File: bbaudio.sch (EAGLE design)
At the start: 35 parts, among them U1 V_REG_MIC2920, U2 V_REG_MIC2920, U3 LMZ14203

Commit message: Some more tewaks to the power section
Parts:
- removed C3: 1uF, rcl:C-EUC0603
- removed C4: 10uF, sparkfun:CAP_POL1206
- removed U1: V_REG_MIC2920, sparkfun:V_REG_MIC2920
- added C10: 10uF, sparkfun:CAP_POL1206
- added C7: 1uF, rcl:C-EUC0603
- added U4: VREG, nonolith:VREG
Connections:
- new net VCC: C2.+, U2.OUT
- net +12V: now also C1.1, U2.IN
- net 1.8V: now also C7.1, U4.VIN; no longer C4.+, U1.OUT
- net 3.3V: now also C10.+, U4.VO; no longer C2.+, C3.1, U1.IN, U2.OUT
- net 5V: no longer C1.1, U2.IN
- net GND: now also C10.-, C7.2, U4.GND; no longer C3.2, C4.-, U1.GND
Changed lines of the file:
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@@
 <part name="R9" library="SparkFun-Passives" deviceset="RESISTOR" device="0603-RES" value="56"/>
 <part name="FRAME1" library="SparkFun-Aesthetics" deviceset="FRAME-LETTER" device=""/>
-<part name="C3" library="rcl" deviceset="C-EU" device="C0603" value="1uF"/>
-<part name="C4" library="sparkfun" deviceset="CAP_POL" device="1206" value="10uF"/>
-<part name="GND7" library="sparkfun" deviceset="GND" device=""/>
-<part name="P+5" library="sparkfun" deviceset="3.3V" device=""/>
-<part name="U1" library="sparkfun" deviceset="V_REG_MIC2920" device=""/>
 <part name="U$10" library="sparkfun" deviceset="1.8V" device=""/>
 <part name="C1" library="rcl" deviceset="C-EU" device="C0603" value="1uF"/>
 <part name="C2" library="sparkfun" deviceset="CAP_POL" device="1206" value="10uF"/>
 <part name="GND2" library="sparkfun" deviceset="GND" device=""/>
-<part name="P+1" library="sparkfun" deviceset="3.3V" device=""/>
 <part name="U2" library="sparkfun" deviceset="V_REG_MIC2920" device=""/>
-<part name="U$3" library="sparkfun" deviceset="5V" device=""/>
 <part name="U3" library="SparkFun-PowerIC" deviceset="LMZ14203" device=""/>
 <part name="C5" library="sparkfun" deviceset="CAP_POL" device="1206" value="10uF"/>
@@
 <part name="R4" library="SparkFun-Passives" deviceset="RESISTOR" device="0603-RES" value="1.07k"/>
 <part name="U$4" library="sparkfun" deviceset="5V" device=""/>
+<part name="P+7" library="supply1" deviceset="+12V" device=""/>
+<part name="P+1" library="supply1" deviceset="VCC" device="" value="AVCC"/>
+<part name="C7" library="rcl" deviceset="C-EU" device="C0603" value="1uF"/>
+<part name="C10" library="sparkfun" deviceset="CAP_POL" device="1206" value="10uF"/>
+<part name="GND12" library="sparkfun" deviceset="GND" device=""/>
+<part name="P+8" library="sparkfun" deviceset="3.3V" device=""/>
+<part name="U4" library="nonolith" deviceset="VREG" device=""/>
+<part name="GND13" library="sparkfun" deviceset="GND" device=""/>
 </parts>
 <sheets>
@@
 <instance part="FRAME1" gate="G$1" x="-78.74" y="-109.22"/>
 <instance part="FRAME1" gate="G$2" x="68.58" y="-109.22"/>
-<instance part="C3" gate="G$1" x="-25.4" y="-142.24"/>
-<instance part="C4" gate="G$1" x="0" y="-142.24"/>
-<instance part="GND7" gate="1" x="-12.7" y="-154.94"/>
-<instance part="P+5" gate="G$1" x="-25.4" y="-129.54" rot="MR0"/>
-<instance part="U1" gate="G$1" x="-12.7" y="-134.62"/>
-<instance part="U$10" gate="G$1" x="0" y="-129.54"/>
+<instance part="U$10" gate="G$1" x="-30.48" y="-127"/>
 <instance part="C1" gate="G$1" x="-73.66" y="-142.24"/>
 <instance part="C2" gate="G$1" x="-48.26" y="-142.24"/>
 <instance part="GND2" gate="1" x="-60.96" y="-154.94"/>
-<instance part="P+1" gate="G$1" x="-48.26" y="-129.54" rot="MR0"/>
 <instance part="U2" gate="G$1" x="-60.96" y="-134.62"/>
-<instance part="U$3" gate="G$1" x="-73.66" y="-129.54"/>
 <instance part="U3" gate="G$1" x="-40.64" y="-185.42"/>
 <instance part="C5" gate="G$1" x="-76.2" y="-200.66"/>
@@
 <instance part="R4" gate="G$1" x="-17.78" y="-203.2" rot="R90"/>
 <instance part="U$4" gate="G$1" x="0" y="-172.72"/>
+<instance part="P+7" gate="1" x="-73.66" y="-127"/>
+<instance part="P+1" gate="VCC" x="-48.26" y="-127"/>
+<instance part="C7" gate="G$1" x="-30.48" y="-142.24"/>
+<instance part="C10" gate="G$1" x="-2.54" y="-142.24"/>
+<instance part="GND12" gate="1" x="-17.78" y="-154.94"/>
+<instance part="P+8" gate="G$1" x="-2.54" y="-127" rot="MR0"/>
+<instance part="U4" gate="G$1" x="-17.78" y="-134.62" rot="MR180"/>
+<instance part="GND13" gate="1" x="-5.08" y="-134.62"/>
 </instances>
 <busses>
@@
 <wire x1="137.16" y1="-2.54" x2="157.48" y2="-2.54" width="0.1524" layer="91"/>
 <wire x1="157.48" y1="-2.54" x2="157.48" y2="-7.62" width="0.1524" layer="91"/>
-</segment>
-<segment>
-<wire x1="0" y1="-149.86" x2="0" y2="-147.32" width="0.1524" layer="91"/>
-<wire x1="-12.7" y1="-149.86" x2="0" y2="-149.86" width="0.1524" layer="91"/>
-<wire x1="-12.7" y1="-149.86" x2="-12.7" y2="-152.4" width="0.1524" layer="91"/>
-<wire x1="-12.7" y1="-149.86" x2="-25.4" y2="-149.86" width="0.1524" layer="91"/>
-<wire x1="-25.4" y1="-149.86" x2="-25.4" y2="-147.32" width="0.1524" layer="91"/>
-<wire x1="-12.7" y1="-142.24" x2="-12.7" y2="-149.86" width="0.1524" layer="91"/>
-<junction x="-12.7" y="-149.86"/>
-<pinref part="C3" gate="G$1" pin="2"/>
-<pinref part="GND7" gate="1" pin="GND"/>
-<pinref part="C4" gate="G$1" pin="-"/>
-<pinref part="U1" gate="G$1" pin="GND"/>
 </segment>
 <segment>
@@
 <wire x1="0" y1="-190.5" x2="0" y2="-200.66" width="0.1524" layer="91"/>
 </segment>
+<segment>
+<wire x1="-2.54" y1="-149.86" x2="-2.54" y2="-147.32" width="0.1524" layer="91"/>
+<wire x1="-17.78" y1="-149.86" x2="-2.54" y2="-149.86" width="0.1524" layer="91"/>
+<wire x1="-17.78" y1="-149.86" x2="-17.78" y2="-152.4" width="0.1524" layer="91"/>
+<wire x1="-17.78" y1="-149.86" x2="-30.48" y2="-149.86" width="0.1524" layer="91"/>
+<wire x1="-30.48" y1="-149.86" x2="-30.48" y2="-147.32" width="0.1524" layer="91"/>
+<junction x="-17.78" y="-149.86"/>
+<pinref part="C7" gate="G$1" pin="2"/>
+<pinref part="GND12" gate="1" pin="GND"/>
+<pinref part="C10" gate="G$1" pin="-"/>
+</segment>
+<segment>
+<wire x1="-7.62" y1="-132.08" x2="-5.08" y2="-132.08" width="0.1524" layer="91"/>
+<pinref part="U4" gate="G$1" pin="GND"/>
+<pinref part="GND13" gate="1" pin="GND"/>
+</segment>
 </net>
 <net name="1.8V" class="0">
@@
 </segment>
 <segment>
-<wire x1="0" y1="-139.7" x2="0" y2="-134.62" width="0.1524" layer="91"/>
-<wire x1="0" y1="-134.62" x2="-5.08" y2="-134.62" width="0.1524" layer="91"/>
-<pinref part="C4" gate="G$1" pin="+"/>
-<pinref part="U1" gate="G$1" pin="OUT"/>
+<wire x1="-30.48" y1="-139.7" x2="-30.48" y2="-134.62" width="0.1524" layer="91"/>
+<wire x1="-30.48" y1="-134.62" x2="-27.94" y2="-134.62" width="0.1524" layer="91"/>
+<pinref part="C7" gate="G$1" pin="1"/>
+<pinref part="U4" gate="G$1" pin="VIN"/>
 <pinref part="U$10" gate="G$1" pin="1.8V"/>
-<wire x1="0" y1="-129.54" x2="0" y2="-134.62" width="0.1524" layer="91"/>
-<junction x="0" y="-134.62"/>
+<wire x1="-30.48" y1="-127" x2="-30.48" y2="-134.62" width="0.1524" layer="91"/>
+<junction x="-30.48" y="-134.62"/>
 </segment>
 </net>
@@
 </segment>
 <segment>
-<wire x1="-25.4" y1="-139.7" x2="-25.4" y2="-134.62" width="0.1524" layer="91"/>
-<wire x1="-25.4" y1="-134.62" x2="-20.32" y2="-134.62" width="0.1524" layer="91"/>
-<pinref part="C3" gate="G$1" pin="1"/>
-<pinref part="U1" gate="G$1" pin="IN"/>
-<pinref part="P+5" gate="G$1" pin="3.3V"/>
-<wire x1="-25.4" y1="-129.54" x2="-25.4" y2="-134.62" width="0.1524" layer="91"/>
-<junction x="-25.4" y="-134.62"/>
-</segment>
-<segment>
-<wire x1="-48.26" y1="-139.7" x2="-48.26" y2="-134.62" width="0.1524" layer="91"/>
-<wire x1="-48.26" y1="-134.62" x2="-53.34" y2="-134.62" width="0.1524" layer="91"/>
-<pinref part="C2" gate="G$1" pin="+"/>
-<pinref part="U2" gate="G$1" pin="OUT"/>
-<pinref part="P+1" gate="G$1" pin="3.3V"/>
-<wire x1="-48.26" y1="-129.54" x2="-48.26" y2="-134.62" width="0.1524" layer="91"/>
-<junction x="-48.26" y="-134.62"/>
+<wire x1="-2.54" y1="-139.7" x2="-2.54" y2="-137.16" width="0.1524" layer="91"/>
+<wire x1="-7.62" y1="-137.16" x2="-2.54" y2="-137.16" width="0.1524" layer="91"/>
+<junction x="-2.54" y="-137.16"/>
+<pinref part="C10" gate="G$1" pin="+"/>
+<pinref part="U4" gate="G$1" pin="VO"/>
+<pinref part="P+8" gate="G$1" pin="3.3V"/>
+<wire x1="-2.54" y1="-127" x2="-2.54" y2="-137.16" width="0.1524" layer="91"/>
 </segment>
 </net>
@@
 <pinref part="U$7" gate="G$1" pin="5V"/>
 <wire x1="81.28" y1="-7.62" x2="71.12" y2="-7.62" width="0.1524" layer="91"/>
-</segment>
-<segment>
-<wire x1="-73.66" y1="-139.7" x2="-73.66" y2="-134.62" width="0.1524" layer="91"/>
-<wire x1="-73.66" y1="-134.62" x2="-68.58" y2="-134.62" width="0.1524" layer="91"/>
-<pinref part="C1" gate="G$1" pin="1"/>
-<pinref part="U2" gate="G$1" pin="IN"/>
-<pinref part="U$3" gate="G$1" pin="5V"/>
-<wire x1="-73.66" y1="-129.54" x2="-73.66" y2="-134.62" width="0.1524" layer="91"/>
-<junction x="-73.66" y="-134.62"/>
 </segment>
 <segment>
@@
 <junction x="-76.2" y="-193.04"/>
 </segment>
+<segment>
+<wire x1="-73.66" y1="-139.7" x2="-73.66" y2="-134.62" width="0.1524" layer="91"/>
+<wire x1="-73.66" y1="-134.62" x2="-68.58" y2="-134.62" width="0.1524" layer="91"/>
+<pinref part="C1" gate="G$1" pin="1"/>
+<pinref part="U2" gate="G$1" pin="IN"/>
+<pinref part="P+7" gate="1" pin="+12V"/>
+<wire x1="-73.66" y1="-129.54" x2="-73.66" y2="-134.62" width="0.1524" layer="91"/>
+<junction x="-73.66" y="-134.62"/>
+</segment>
 </net>
 <net name="N$6" class="0">
@@
 </segment>
 </net>
+<net name="VCC" class="0">
+<segment>
+<wire x1="-48.26" y1="-139.7" x2="-48.26" y2="-134.62" width="0.1524" layer="91"/>
+<wire x1="-48.26" y1="-134.62" x2="-53.34" y2="-134.62" width="0.1524" layer="91"/>
+<pinref part="C2" gate="G$1" pin="+"/>
+<pinref part="U2" gate="G$1" pin="OUT"/>
+<pinref part="P+1" gate="VCC" pin="VCC"/>
+<wire x1="-48.26" y1="-129.54" x2="-48.26" y2="-134.62" width="0.1524" layer="91"/>
+<junction x="-48.26" y="-134.62"/>
+</segment>
+</net>

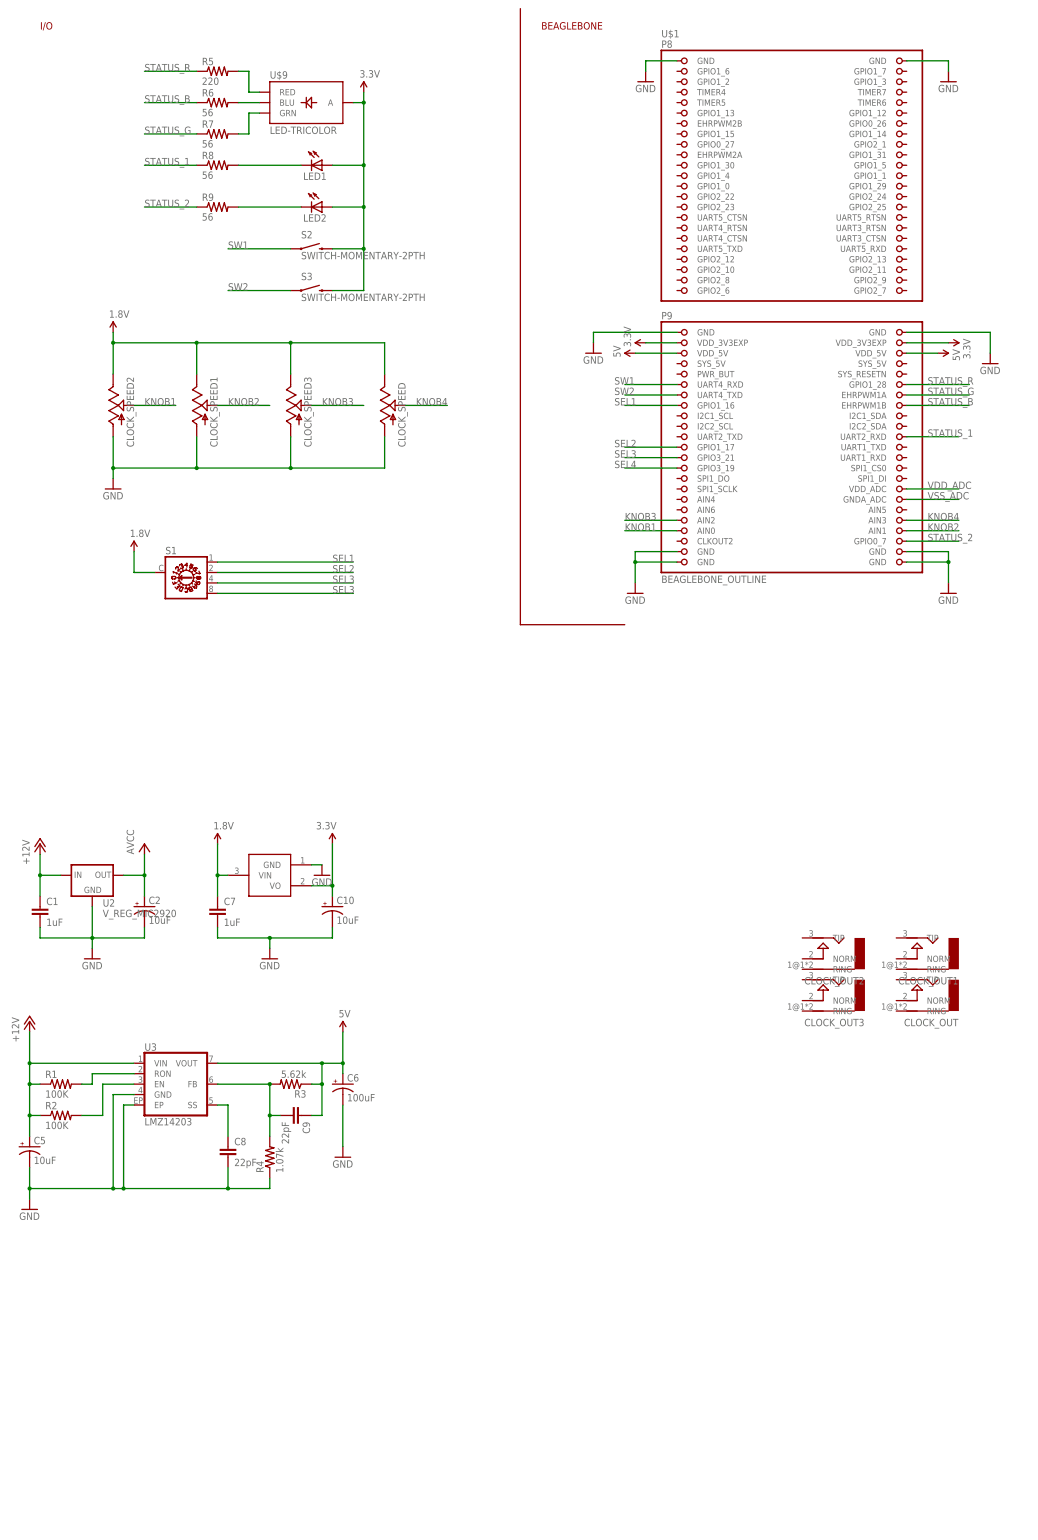
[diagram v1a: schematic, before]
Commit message: Added codec and power connector
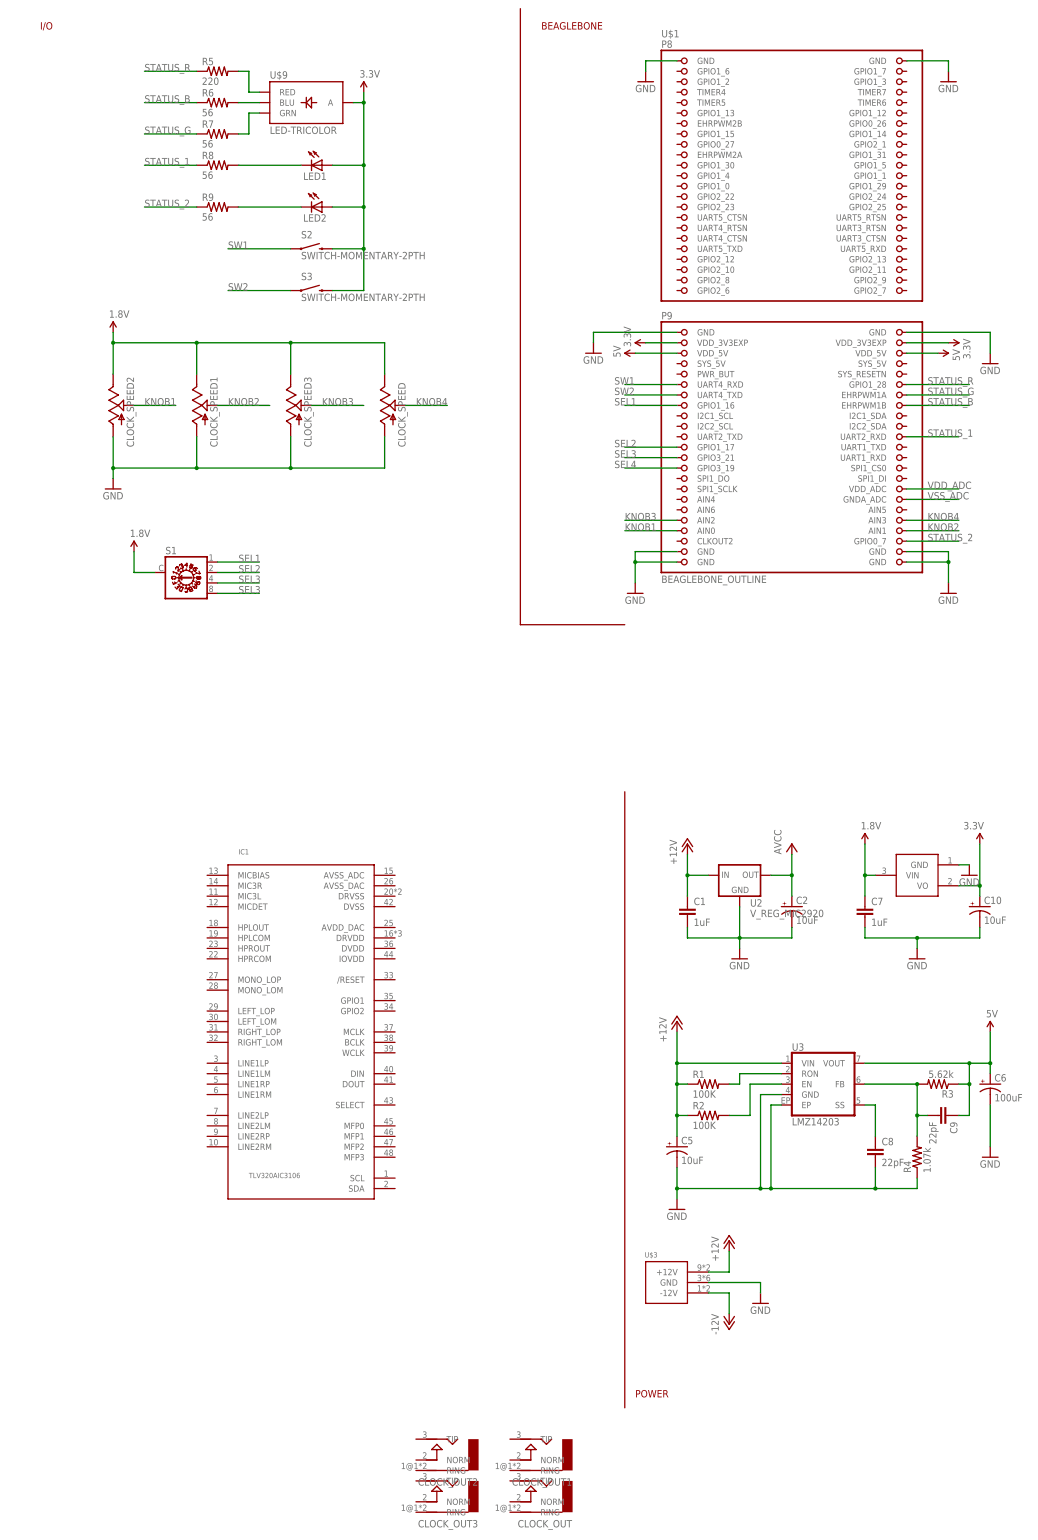
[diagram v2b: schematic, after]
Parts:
- added IC1: TLV320AIC3106, codec:TLV320AIC3106
- added U$3: POWER_SIMPLE10, eurorack:POWER_SIMPLE10
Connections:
- new net -12V: U$3.-12V
- net +12V: now also U$3.+12V
- net GND: now also U$3.GND
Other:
- note added: "POWER"
- moved on the sheet: C1, C10, C2, C5, C6, C7, C8, C9, CLOCK_OUT, CLOCK_OUT1, CLOCK_OUT2, CLOCK_OUT3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

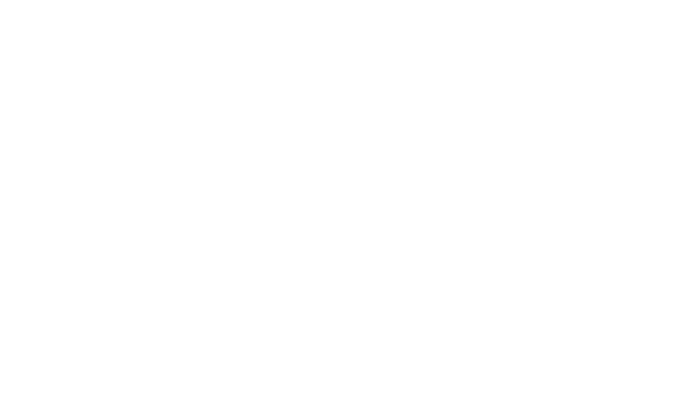
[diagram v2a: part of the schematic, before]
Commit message: Added clock source
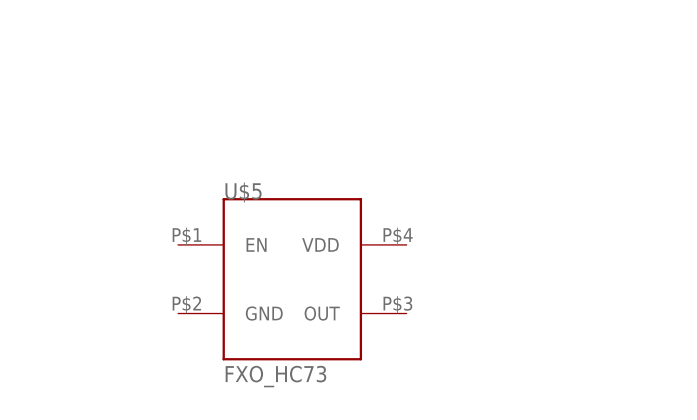
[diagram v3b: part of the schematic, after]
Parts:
- added U$5: FXO_HC73, codec:FXO_HC73
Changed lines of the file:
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@@
 <part name="P-1" library="supply1" deviceset="-12V" device=""/>
 <part name="GND7" library="sparkfun" deviceset="GND" device=""/>
+<part name="U$5" library="codec" deviceset="FXO_HC73" device=""/>
 </parts>
 <sheets>
@@
 <instance part="P-1" gate="1" x="93.98" y="-243.84"/>
 <instance part="GND7" gate="1" x="101.6" y="-238.76"/>
+<instance part="U$5" gate="G$1" x="-43.18" y="-279.4"/>
 </instances>
 <busses>
